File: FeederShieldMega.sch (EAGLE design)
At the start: 44 parts, among them J1 Digital_0_7, J10 Power, J2 Analog, J3 Digital_8_13, J4 Analog, J5 Digital_0_7, J6 Digital_22_36, J7 Digital_23_37, J8 Digital_38_52, J9 Digital_39_53, Q2 NTD5867NLT4G

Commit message: Tweaks for v1.0 release
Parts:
- JP23: value N20 -> (none)
- JP24: value N21 -> (none)
- JP25: value N22 -> (none)
- JP26: value N23 -> (none)
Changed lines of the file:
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@@
 <part name="JP21" library="freetronics-jon" deviceset="M04" device="PTH" value="N18"/>
 <part name="JP22" library="freetronics-jon" deviceset="M04" device="PTH" value="N19"/>
-<part name="JP23" library="freetronics-jon" deviceset="M04" device="PTH" value="N20"/>
-<part name="JP24" library="freetronics-jon" deviceset="M04" device="PTH" value="N21"/>
-<part name="JP25" library="freetronics-jon" deviceset="M04" device="PTH" value="N22"/>
-<part name="JP26" library="freetronics-jon" deviceset="M04" device="PTH" value="N23"/>
+<part name="JP23" library="freetronics-jon" deviceset="M04" device="PTH"/>
+<part name="JP24" library="freetronics-jon" deviceset="M04" device="PTH"/>
+<part name="JP25" library="freetronics-jon" deviceset="M04" device="PTH"/>
+<part name="JP26" library="freetronics-jon" deviceset="M04" device="PTH"/>
 <part name="Q2" library="freetronics-master-v1.1" deviceset="MOSFET-NCHANNEL" device="DPAK" value="NTD5867NLT4G"/>
 <part name="GND2" library="freetronics-original" deviceset="GND" device=""/>

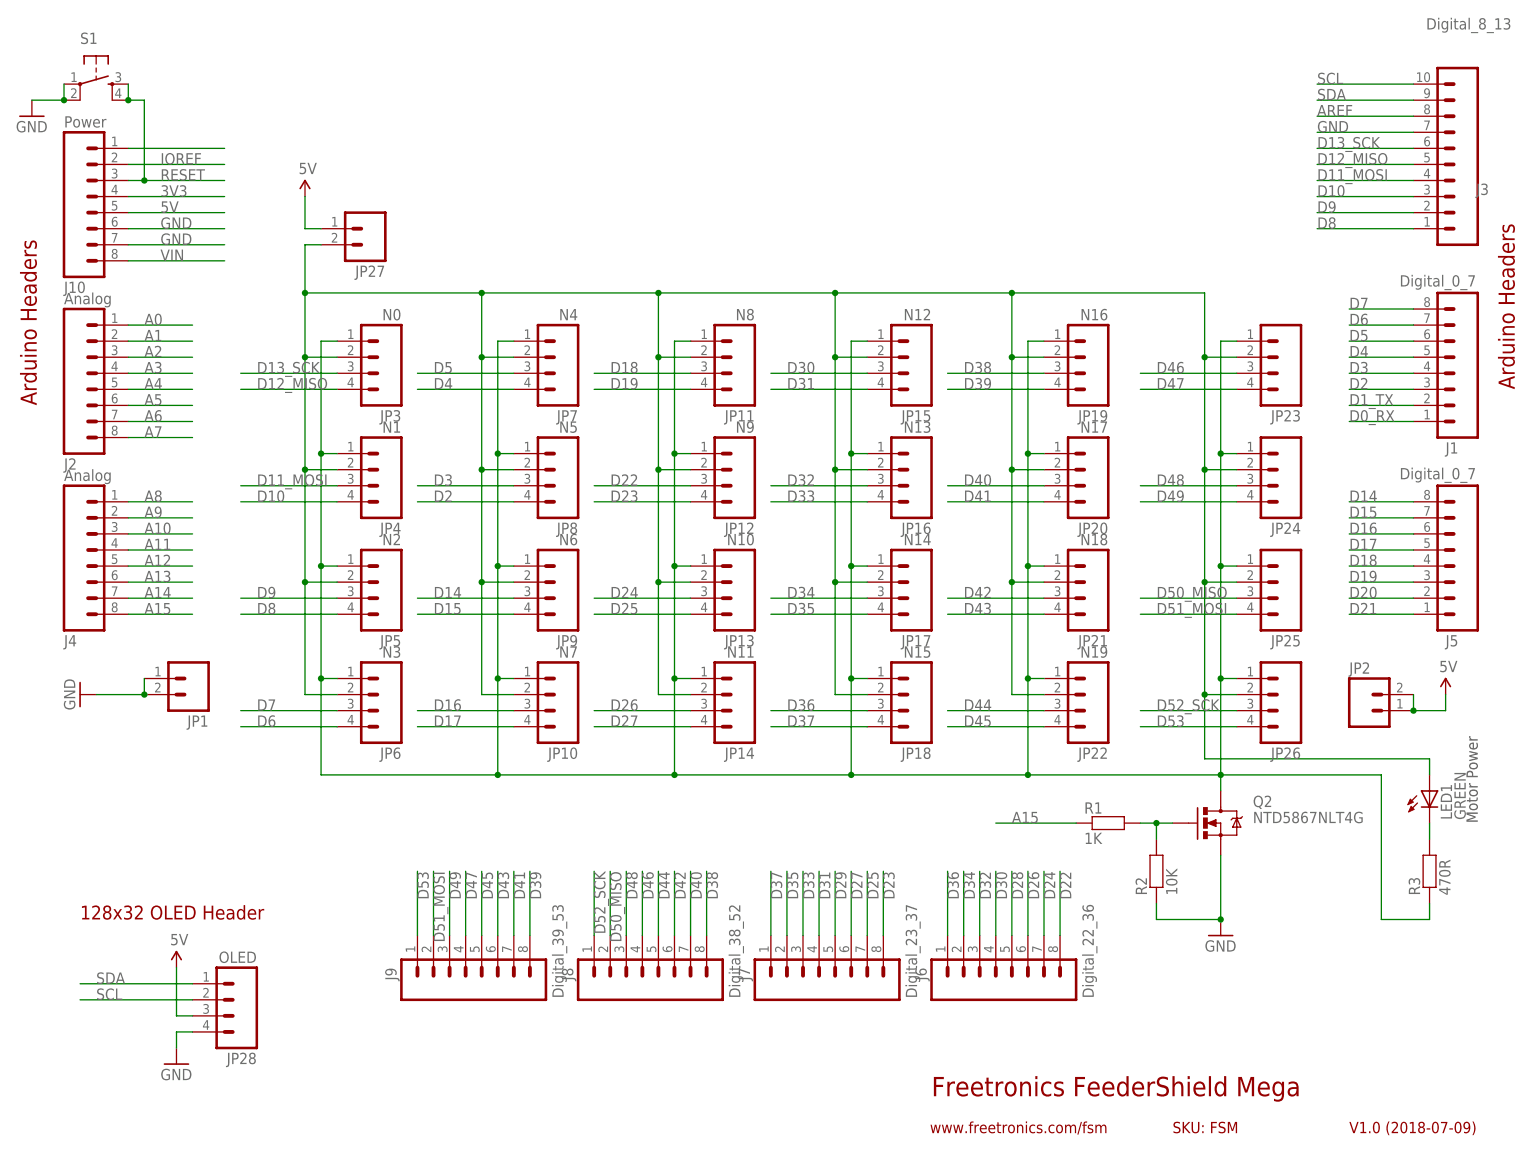
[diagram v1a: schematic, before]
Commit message: Major rework to use 10-way IDC connections for v2.0 release
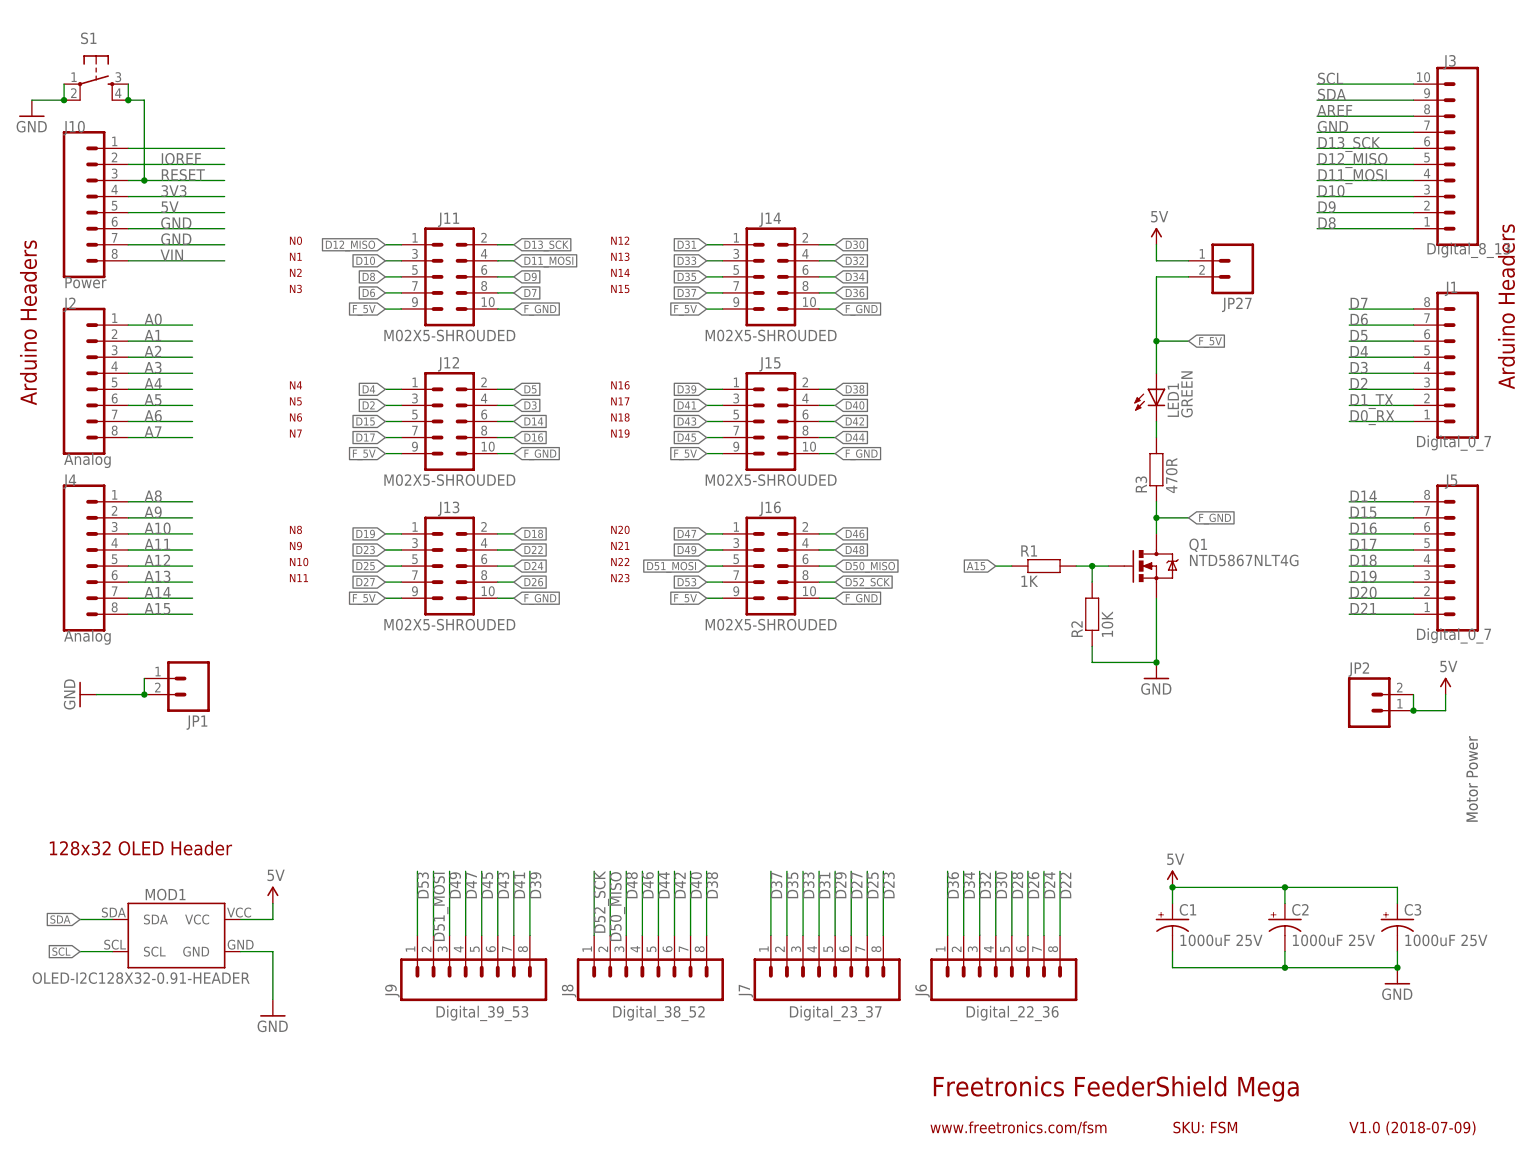
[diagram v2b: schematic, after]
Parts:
- removed JP10: N7, freetronics-jon:M04PTH
- removed JP11: N8, freetronics-jon:M04PTH
- removed JP12: N9, freetronics-jon:M04PTH
- removed JP13: N10, freetronics-jon:M04PTH
- removed JP14: N11, freetronics-jon:M04PTH
- removed JP15: N12, freetronics-jon:M04PTH
- removed JP16: N13, freetronics-jon:M04PTH
- removed JP17: N14, freetronics-jon:M04PTH
- removed JP18: N15, freetronics-jon:M04PTH
- removed JP19: N16, freetronics-jon:M04PTH
- removed JP20: N17, freetronics-jon:M04PTH
- removed JP21: N18, freetronics-jon:M04PTH
- removed JP22: N19, freetronics-jon:M04PTH
- removed JP23, JP24, JP25, JP26: (no value), freetronics-jon:M04PTH
- removed JP28: OLED, freetronics-jon:M04PTH
- removed JP3: N0, freetronics-jon:M04PTH
- removed JP4: N1, freetronics-jon:M04PTH
- removed JP5: N2, freetronics-jon:M04PTH
- removed JP6: N3, freetronics-jon:M04PTH
- removed JP7: N4, freetronics-jon:M04PTH
- removed JP8: N5, freetronics-jon:M04PTH
- removed JP9: N6, freetronics-jon:M04PTH
- removed Q2: NTD5867NLT4G, freetronics-master-v1.1:MOSFET-NCHANNELDPAK
- added C1, C2, C3: 1000uF 25V, SuperHouse-DiscreteSemi:CAP_POL-5.08-10X18-FLAT
- added J11, J12, J13, J14, J15, J16: M02X5-SHROUDED, SuperHouse-Connectors:M02X5-SHROUDED
- added MOD1: OLED-I2C128X32-0.91-HEADER, SuperHouse-Displays:OLED-I2C128X32-0.91-HEADER
- added Q1: NTD5867NLT4G, SuperHouse-DiscreteSemi:MOSFET-NCHANNEL-DPAK
- J1, J5, J6, J7, J8, J9: device freetronics:M08 -> SuperHouse-Connectors:M08-PIN-BELOW
- J10, J2, J4: device freetronics-master-v1:M08 -> SuperHouse-Connectors:M08-PIN-BELOW
- J3: device freetronics-original:M100.1 -> SuperHouse-Connectors:M10-PIN-BELOW
- JP1, JP2: device freetronics-master-v1:M02PTH -> SuperHouse-Connectors:M02-PIN-BELOW
- JP27: device freetronics-jon:M02PTH -> SuperHouse-Connectors:M02-PIN
- LED1: device freetronics-jon:LED0603 -> SuperHouse-LEDs:LED0603
- R1, R2, R3: device freetronics-jon:RESISTOR0603 -> SuperHouse-DiscreteSemi:RESISTOR0603
- S1: device freetronics-master-v1:TAC_SWITCHPTH -> SuperHouse-Switches:TAC_SWITCH-PTH-6
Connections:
- removed net N$1: JP10.1, JP11.1, JP12.1, JP13.1, JP14.1, JP15.1, JP16.1, JP17.1, JP18.1, JP19.1, JP20.1, JP21.1, JP22.1, JP23.1, JP24.1, JP25.1, JP26.1, JP3.1, JP4.1, JP5.1, JP6.1, JP7.1, JP8.1, JP9.1, Q2.D, R3.1
- removed net N$2: JP10.2, JP11.2, JP12.2, JP13.2, JP14.2, JP15.2, JP16.2, JP17.2, JP18.2, JP19.2, JP20.2, JP21.2, JP22.2, JP23.2, JP24.2, JP25.2, JP26.2, JP27.2, JP3.2, JP4.2, JP5.2, JP6.2, JP7.2, JP8.2, JP9.2, LED1.A
- new net F_5V: J11.9, J12.9, J13.9, J14.9, J15.9, J16.9, JP27.2, LED1.A
- new net F_GND: J11.10, J12.10, J13.10, J14.10, J15.10, J16.10, Q1.D, R3.1
- net 5V: now also C1.+, C2.+, C3.+, MOD1.VCC; no longer JP28.3
- net D10: now also J11.3; no longer JP4.4
- net D11_MOSI: now also J11.4; no longer JP4.3
- net D12_MISO: now also J11.1; no longer JP3.4
- net D13_SCK: now also J11.2; no longer JP3.3
- net D14: now also J12.6; no longer JP9.3
- net D15: now also J12.5; no longer JP9.4
- net D16: now also J12.8; no longer JP10.3
- net D17: now also J12.7; no longer JP10.4
- net D18: now also J13.2; no longer JP11.3
- net D19: now also J13.1; no longer JP11.4
- net D2: now also J12.3; no longer JP8.4
- net D22: now also J13.4; no longer JP12.3
- net D23: now also J13.3; no longer JP12.4
- net D24: now also J13.6; no longer JP13.3
- net D25: now also J13.5; no longer JP13.4
- net D26: now also J13.8; no longer JP14.3
- net D27: now also J13.7; no longer JP14.4
- net D3: now also J12.4; no longer JP8.3
- net D30: now also J14.2; no longer JP15.3
- net D31: now also J14.1; no longer JP15.4
- net D32: now also J14.4; no longer JP16.3
- net D33: now also J14.3; no longer JP16.4
- net D34: now also J14.6; no longer JP17.3
- net D35: now also J14.5; no longer JP17.4
- net D36: now also J14.8; no longer JP18.3
- net D37: now also J14.7; no longer JP18.4
- net D38: now also J15.2; no longer JP19.3
- net D39: now also J15.1; no longer JP19.4
- net D4: now also J12.1; no longer JP7.4
- net D40: now also J15.4; no longer JP20.3
- net D41: now also J15.3; no longer JP20.4
- net D42: now also J15.6; no longer JP21.3
- net D43: now also J15.5; no longer JP21.4
- net D44: now also J15.8; no longer JP22.3
- net D45: now also J15.7; no longer JP22.4
- net D46: now also J16.2; no longer JP23.3
- net D47: now also J16.1; no longer JP23.4
- net D48: now also J16.4; no longer JP24.3
- net D49: now also J16.3; no longer JP24.4
- net D5: now also J12.2; no longer JP7.3
- net D50_MISO: now also J16.6; no longer JP25.3
- net D51_MOSI: now also J16.5; no longer JP25.4
- net D52_SCK: now also J16.8; no longer JP26.3
- net D53: now also J16.7; no longer JP26.4
- net D6: now also J11.7; no longer JP6.4
- net D7: now also J11.8; no longer JP6.3
- net D8: now also J11.5; no longer JP5.4
- net D9: now also J11.6; no longer JP5.3
- net GND: now also C1.-, C2.-, C3.-, MOD1.GND, Q1.S; no longer JP28.4, Q2.S
- net N$3: now also Q1.G; no longer Q2.G
- net SCL: now also MOD1.SCL; no longer JP28.2
- net SDA: now also MOD1.SDA; no longer JP28.1
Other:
- note added: "N0"
- note added: "N1"
- note added: "N10"
- note added: "N11"
- note added: "N12"
- note added: "N13"
- note added: "N14"
- note added: "N15"
- note added: "N16"
- note added: "N17"
- note added: "N18"
- note added: "N19"
- note added: "N2"
- note added: "N20"
- note added: "N21"
- note added: "N22"
- note added: "N23"
- note added: "N3"
- note added: "N4"
- note added: "N5"
- note added: "N6"
- note added: "N7"
- note added: "N8"
- note added: "N9"
- moved on the sheet: JP27, LED1, R1, R2, R3
